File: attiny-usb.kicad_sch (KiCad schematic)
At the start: 12 parts, among them J1 Conn_01x05, U1 ATtiny85-20P

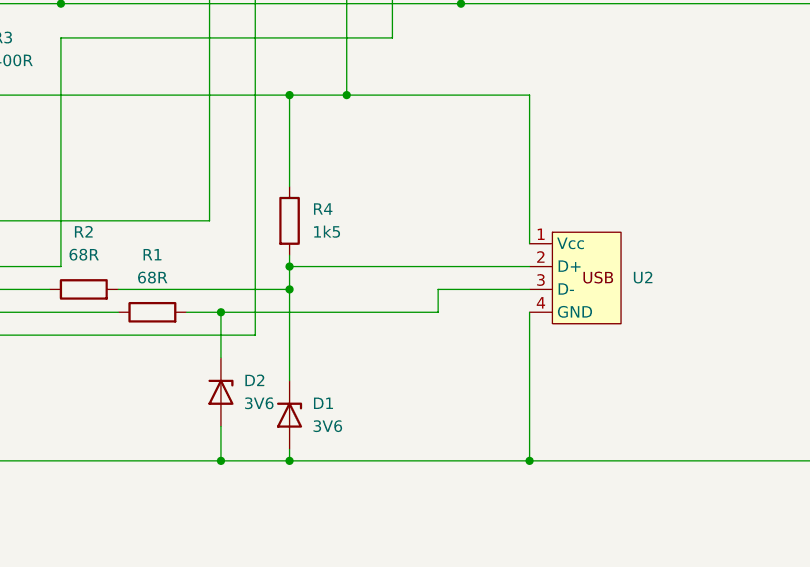
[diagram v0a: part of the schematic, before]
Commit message: create 2x3 panel
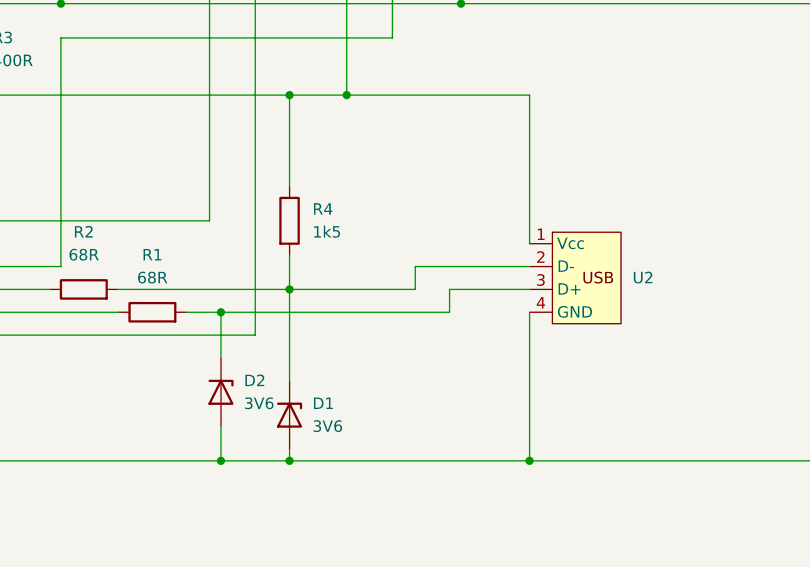
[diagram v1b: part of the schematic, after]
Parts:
- C1, C2: JLC 1206 -> 0805; LCSC C525187 -> C495959
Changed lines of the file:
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@@
   (junction (at 158.75 128.27) (diameter 0) (color 0 0 0 0)
   )
-  (junction (at 158.75 106.68) (diameter 0) (color 0 0 0 0)
-  )
   (junction (at 88.9 128.27) (diameter 0) (color 0 0 0 0)
   )
@@
   (junction (at 88.9 87.63) (diameter 0) (color 0 0 0 0)
   )
+  (junction (at 151.13 111.76) (diameter 0) (color 0 0 0 0)
+  )
   (junction (at 165.1 87.63) (diameter 0) (color 0 0 0 0)
   )
-  (junction (at 151.13 111.76) (diameter 0) (color 0 0 0 0)
-  )
   (junction (at 96.52 87.63) (diameter 0) (color 0 0 0 0)
   )
@@
     (stroke (width 0) (type default))
   )
-  (wire (pts (xy 158.75 106.68) (xy 185.42 106.68))
-    (stroke (width 0) (type default))
-  )
   (wire (pts (xy 133.35 106.68) (xy 133.35 81.28))
     (stroke (width 0) (type default))
@@
     (stroke (width 0) (type default))
   )
-  (wire (pts (xy 158.75 106.68) (xy 158.75 109.22))
+  (wire (pts (xy 158.75 105.41) (xy 158.75 109.22))
     (stroke (width 0) (type default))
   )
@@
     (stroke (width 0) (type default))
   )
-  (wire (pts (xy 175.26 111.76) (xy 175.26 109.22))
-    (stroke (width 0) (type default))
-  )
   (wire (pts (xy 133.35 54.61) (xy 113.03 54.61))
     (stroke (width 0) (type default))
@@
     (stroke (width 0) (type default))
   )
+  (wire (pts (xy 176.53 111.76) (xy 176.53 109.22))
+    (stroke (width 0) (type default))
+  )
   (wire (pts (xy 104.14 101.6) (xy 149.86 101.6))
     (stroke (width 0) (type default))
@@
     (stroke (width 0) (type default))
   )
+  (wire (pts (xy 172.72 106.68) (xy 185.42 106.68))
+    (stroke (width 0) (type default))
+  )
   (wire (pts (xy 165.1 87.63) (xy 158.75 87.63))
     (stroke (width 0) (type default))
   )
-  (wire (pts (xy 175.26 109.22) (xy 185.42 109.22))
+  (wire (pts (xy 176.53 109.22) (xy 185.42 109.22))
     (stroke (width 0) (type default))
   )
@@
     (stroke (width 0) (type default))
   )
+  (wire (pts (xy 158.75 109.22) (xy 172.72 109.22))
+    (stroke (width 0) (type default))
+  )
   (wire (pts (xy 154.94 64.77) (xy 179.07 64.77))
     (stroke (width 0) (type default))
   )
-  (wire (pts (xy 158.75 105.41) (xy 158.75 106.68))
-    (stroke (width 0) (type default))
-  )
   (wire (pts (xy 88.9 87.63) (xy 88.9 93.98))
     (stroke (width 0) (type default))
@@
     (stroke (width 0) (type default))
   )
+  (wire (pts (xy 172.72 109.22) (xy 172.72 106.68))
+    (stroke (width 0) (type default))
+  )
   (wire (pts (xy 151.13 128.27) (xy 88.9 128.27))
     (stroke (width 0) (type default))
@@
     (stroke (width 0) (type default))
   )
+  (wire (pts (xy 151.13 111.76) (xy 176.53 111.76))
+    (stroke (width 0) (type default))
+  )
   (wire (pts (xy 113.03 69.85) (xy 113.03 77.47))
     (stroke (width 0) (type default))
   )
-  (wire (pts (xy 151.13 111.76) (xy 175.26 111.76))
-    (stroke (width 0) (type default))
-  )
   (wire (pts (xy 104.14 106.68) (xy 133.35 106.68))
     (stroke (width 0) (type default))
@@
         (path "/9c4cbead-451c-4296-96c8-5529617eee01"
           (reference "R3") (unit 1)
+        )
+      )
+    )
+  )
+  (symbol (lib_id "my_lib:pcb_usb-connector") (at 185.42 107.95 0) (unit 1)
+    (in_bom yes) (on_board yes) (dnp no) (fields_autoplaced)
+    (property "Reference" "U2" (at 196.85 107.95 0)
+      (effects (font (size 1.27 1.27)) (justify left))
+    )
+    (property "Value" "~" (at 185.42 107.95 0)
+      (effects (font (size 1.27 1.27)))
+    )
+    (property "Footprint" "my_lib:pcb_usb-connector" (at 185.42 107.95 0)
+      (effects (font (size 1.27 1.27)) hide)
+    )
+    (property "Datasheet" "" (at 185.42 107.95 0)
+      (effects (font (size 1.27 1.27)) hide)
+    )
+    (pin "1")
+    (pin "2")
+    (pin "3")
+    (pin "4")
+    (instances
+      (project "attiny-usb"
+        (path "/9c4cbead-451c-4296-96c8-5529617eee01"
+          (reference "U2") (unit 1)
         )
       )
@@
         (path "/9c4cbead-451c-4296-96c8-5529617eee01"
           (reference "J1") (unit 1)
-        )
-      )
-    )
-  )
-  (symbol (lib_id "my_lib:pcb_usb-connector") (at 185.42 107.95 0) (unit 1)
-    (in_bom yes) (on_board yes) (dnp no) (fields_autoplaced)
-    (property "Reference" "U2" (at 196.85 107.95 0)
-      (effects (font (size 1.27 1.27)) (justify left))
-    )
-    (property "Value" "~" (at 185.42 107.95 0)
-      (effects (font (size 1.27 1.27)))
-    )
-    (property "Footprint" "my_lib:pcb_usb-connector" (at 185.42 107.95 0)
-      (effects (font (size 1.27 1.27)) hide)
-    )
-    (property "Datasheet" "" (at 185.42 107.95 0)
-      (effects (font (size 1.27 1.27)) hide)
-    )
-    (property "JLC" "" (at 185.42 107.95 0)
-      (effects (font (size 1.27 1.27)) hide)
-    )
-    (property "LCSC" "" (at 185.42 107.95 0)
-      (effects (font (size 1.27 1.27)) hide)
-    )
-    (pin "1")
-    (pin "2")
-    (pin "3")
-    (pin "4")
-    (instances
-      (project "attiny-usb"
-        (path "/9c4cbead-451c-4296-96c8-5529617eee01"
-          (reference "U2") (unit 1)
         )
       )
@@
       (effects (font (size 1.27 1.27)) hide)
     )
-    (property "JLC" "1206" (at 113.03 66.04 0)
-      (effects (font (size 1.27 1.27)) hide)
-    )
-    (property "LCSC" "C525187" (at 113.03 66.04 0)
+    (property "JLC" "0805" (at 113.03 66.04 0)
+      (effects (font (size 1.27 1.27)) hide)
+    )
+    (property "LCSC" "C495959" (at 113.03 66.04 0)
       (effects (font (size 1.27 1.27)) hide)
     )
@@
       (effects (font (size 1.27 1.27)) hide)
     )
-    (property "JLC" "1206" (at 45.72 107.95 0)
-      (effects (font (size 1.27 1.27)) hide)
-    )
-    (property "LCSC" "C525187" (at 45.72 107.95 0)
-      (effects (font (size 1.27 1.27)) hide)
-    )
+    (property "JLC" "0805" (at 45.72 107.95 0)
+      (effects (font (size 1.27 1.27)) hide)
+    )
+    (property "LCSC" "C495959" (at 45.72 107.95 0)
+      (effects (font (size 1.27 1.27)) hide)
+    )

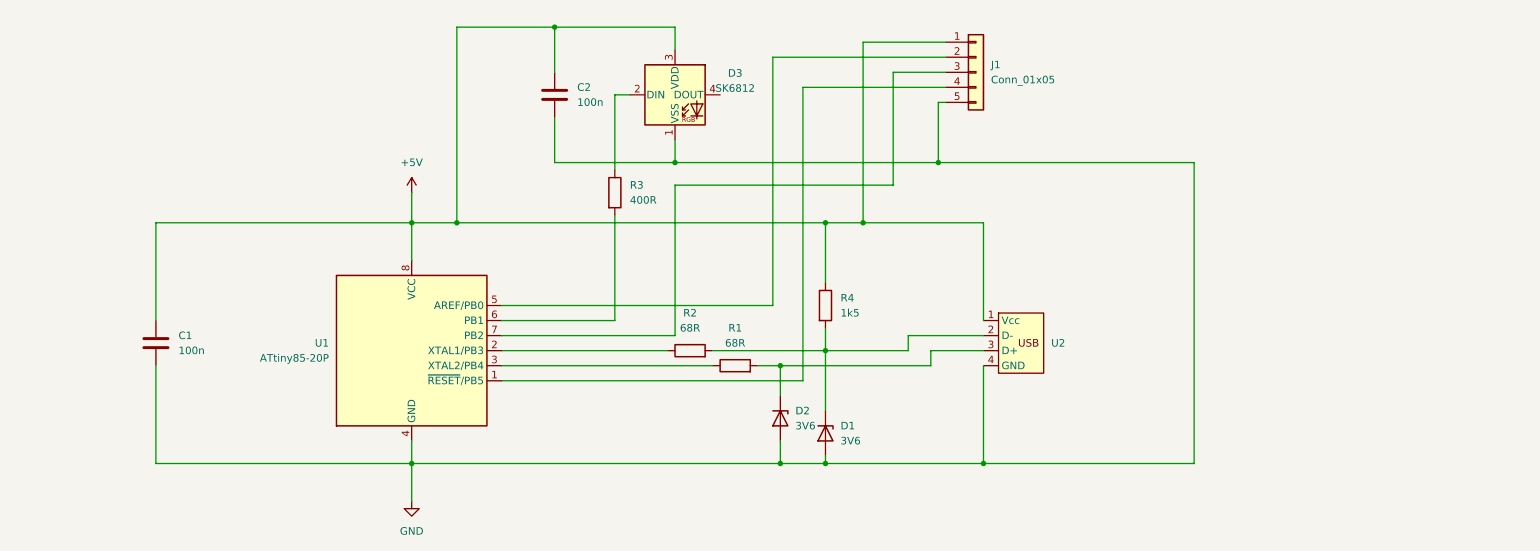
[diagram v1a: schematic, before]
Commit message: create pcb outline for version 2.0.0
Thinking about moving large pin header one step towards the usb
connector.
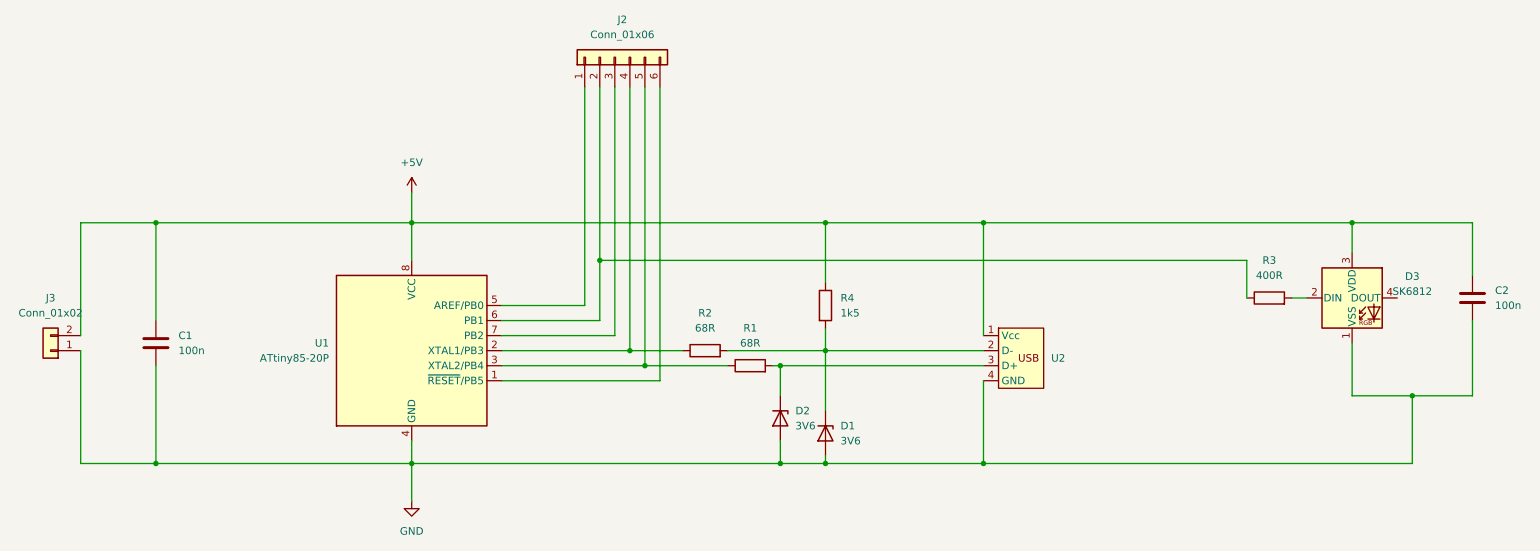
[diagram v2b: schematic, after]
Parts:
- removed J1: Conn_01x05, Connector_PinHeader_2.54mm:PinHeader_1x05_P2.54mm_Vertical, symbol Connector_Generic:Conn_01x05
- added J2: Conn_01x06, Connector_PinHeader_2.54mm:PinHeader_1x06_P2.54mm_Vertical, symbol Connector_Generic:Conn_01x06
- added J3: Conn_01x02, Connector_PinHeader_2.54mm:PinHeader_1x02_P2.54mm_Vertical, symbol Connector_Generic:Conn_01x02
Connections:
- net +5V: now also J3.2 (Pin_2)
- net GND: now also J3.1 (Pin_1)
- net at R2.1, U1.2 (XTAL1/PB3): now also J2.4 (Pin_4)
- net at R3.1: now also U1.6 (PB1), J2.2 (Pin_2); no longer D3.2 (DIN)
- net at R3.2: now also D3.2 (DIN); no longer U1.6 (PB1)
- net at U1.5 (AREF/PB0): now also J2.1 (Pin_1)
- net at U1.7 (PB2): now also J2.3 (Pin_3)
- net at U1.1 (~{RESET}/PB5): now also J2.6 (Pin_6)
- net at R1.1, U1.3 (XTAL2/PB4): now also J2.5 (Pin_5)
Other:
- moved on the sheet: C2, D3, R1, R2, R3, U2

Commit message: move large pin header and remove resistor for Neopixel
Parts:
- removed R3: 400R, Resistor_SMD:R_0805_2012Metric_Pad1.20x1.40mm_HandSolder, symbol Device:R
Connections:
- net at J2.2 (Pin_2), U1.6 (PB1): now also D3.2 (DIN)
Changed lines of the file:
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@@
     (stroke (width 0) (type default))
   )
-  (wire (pts (xy 237.49 100.33) (xy 240.03 100.33))
+  (wire (pts (xy 229.87 100.33) (xy 240.03 100.33))
     (stroke (width 0) (type default))
   )
@@
         )
       )
-    )
-  )
-  (symbol (lib_id "Device:R") (at 233.68 100.33 90) (unit 1)
-    (in_bom yes) (on_board yes) (dnp no) (fields_autoplaced)
-    (property "Reference" "R3" (at 233.68 93.98 90)
-      (effects (font (size 1.27 1.27)))
-    )
-    (property "Value" "400R" (at 233.68 96.52 90)
-      (effects (font (size 1.27 1.27)))
-    )
-    (property "Footprint" "Resistor_SMD:R_0805_2012Metric_Pad1.20x1.40mm_HandSolder" (at 233.68 102.108 90)
-      (effects (font (size 1.27 1.27)) hide)
-    )
-    (property "Datasheet" "~" (at 233.68 100.33 0)
-      (effects (font (size 1.27 1.27)) hide)
-    )
-    (property "JLC" "0805" (at 233.68 100.33 0)
-      (effects (font (size 1.27 1.27)) hide)
-    )
-    (property "LCSC" "C153298" (at 233.68 100.33 0)
-      (effects (font (size 1.27 1.27)) hide)
-    )
-    (pin "1")
-    (pin "2")
-    (instances
-      (project "attiny-usb"
-        (path "/9c4cbead-451c-4296-96c8-5529617eee01"
-          (reference "R3") (unit 1)
-        )
-      )

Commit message: correct footprint of C1,C2 and add header for Neopixel output
fixes #2
fixes #3
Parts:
- added J1: Conn_01x01, Connector_PinHeader_2.54mm:PinHeader_1x01_P2.54mm_Vertical, symbol Connector_Generic:Conn_01x01
- C1, C2: footprint Capacitor_SMD:C_1206_3216Metric_Pad1.33x1.80mm_HandSolder -> Capacitor_SMD:C_0805_2012Metric_Pad1.18x1.45mm_HandSolder
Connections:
- net at D3.4 (DOUT): now also J1.1 (Pin_1)
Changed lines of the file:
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@@
+    (stroke (width 0) (type default))
+  )
+  (wire (pts (xy 255.27 100.33) (xy 255.27 110.49))
     (stroke (width 0) (type default))
   )
@@
     (stroke (width 0) (type default))
   )
+  (wire (pts (xy 255.27 110.49) (xy 256.54 110.49))
+    (stroke (width 0) (type default))
+  )
   (wire (pts (xy 185.42 106.68) (xy 185.42 87.63))
     (stroke (width 0) (type default))
@@
         (path "/9c4cbead-451c-4296-96c8-5529617eee01"
           (reference "R2") (unit 1)
+        )
+      )
+    )
+  )
+  (symbol (lib_id "Connector_Generic:Conn_01x01") (at 261.62 110.49 0) (unit 1)
+    (in_bom yes) (on_board yes) (dnp no) (fields_autoplaced)
+    (property "Reference" "J1" (at 264.16 109.22 0)
+      (effects (font (size 1.27 1.27)) (justify left))
+    )
+    (property "Value" "Conn_01x01" (at 264.16 111.76 0)
+      (effects (font (size 1.27 1.27)) (justify left))
+    )
+    (property "Footprint" "Connector_PinHeader_2.54mm:PinHeader_1x01_P2.54mm_Vertical" (at 261.62 110.49 0)
+      (effects (font (size 1.27 1.27)) hide)
+    )
+    (property "Datasheet" "~" (at 261.62 110.49 0)
+      (effects (font (size 1.27 1.27)) hide)
+    )
+    (pin "1")
+    (instances
+      (project "attiny-usb"
+        (path "/9c4cbead-451c-4296-96c8-5529617eee01"
+          (reference "J1") (unit 1)
         )
       )
@@
       (effects (font (size 1.27 1.27)) (justify left))
     )
-    (property "Footprint" "Capacitor_SMD:C_1206_3216Metric_Pad1.33x1.80mm_HandSolder" (at 268.9352 104.14 0)
+    (property "Footprint" "Capacitor_SMD:C_0805_2012Metric_Pad1.18x1.45mm_HandSolder" (at 268.9352 104.14 0)
       (effects (font (size 1.27 1.27)) hide)
     )
@@
       (effects (font (size 1.27 1.27)) (justify left))
     )
-    (property "Footprint" "Capacitor_SMD:C_1206_3216Metric_Pad1.33x1.80mm_HandSolder" (at 46.6852 111.76 0)
-      (effects (font (size 1.27 1.27)) hide)
-    )
+    (property "Footprint" "Capacitor_SMD:C_0805_2012Metric_Pad1.18x1.45mm_HandSolder" (at 46.6852 111.76 0)
+      (effects (font (size 1.27 1.27)) hide)
+    )
